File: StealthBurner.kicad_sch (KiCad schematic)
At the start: 11 parts, among them J1 PROBE, J2 E-Step, J3 HE, J4 HET, J5 FS, J6 HEF, J7 PCF, J8 LED, J9 MCU

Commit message: 修改设计规范
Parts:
- D1: footprint (none) -> Diode_THT:D_DO-34_SOD68_P2.54mm_Vertical_AnodeUp
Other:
- company: (none) -> LassiCat Organization
- title: (none) -> StealthBurner Toolhead PCB
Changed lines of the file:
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@@
 (kicad_sch (version 20211123) (generator eeschema)
   (paper "A4")
+  (title_block
+    (title "StealthBurner Toolhead PCB")
+    (date "2022-05-24")
+    (rev "Bata0")
+    (company "LassiCat Organization")
+    (comment 1 "Auther: CharlieYu")
+  )
   (wire (pts (xy 130.81 119.38) (xy 135.89 119.38))
     (stroke (width 0) (type default) (color 0 0 0 0))
@@
     (property "Reference" "D1" (id 0) (at 133.35 66.04 0))
     (property "Value" "BAT85" (id 1) (at 134.62 67.31 0))
-    (property "Footprint" "" (id 2) (at 129.54 62.23 0)
-      (effects (font (size 1.27 1.27)) hide)
-    )
+    (property "Footprint" "Diode_THT:D_DO-34_SOD68_P2.54mm_Vertical_AnodeUp" (id 2) (at 129.54 62.23 0)
+      (effects (font (size 1.27 1.27)) hide)
+    )

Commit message: 重新设计 PCB
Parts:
- D1: footprint Diode_THT:D_DO-34_SOD68_P2.54mm_Vertical_AnodeUp -> Diode_THT:D_DO-35_SOD27_P2.54mm_Vertical_AnodeUp
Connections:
- net FS: now also J9.5 (Pin_5); no longer J9.15 (Pin_15)
- net HE+: now also J9.15 (Pin_15); no longer J9.5 (Pin_5)
- net HE-: now also J9.14 (Pin_14); no longer J9.4 (Pin_4)
- net HEF: now also J9.9 (Pin_9); no longer J9.8 (Pin_8)
- net PCF: now also J9.8 (Pin_8); no longer J9.9 (Pin_9)
- net P_SIG: now also J9.4 (Pin_4); no longer J9.14 (Pin_14)
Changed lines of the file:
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@@
     (effects (font (size 1.27 1.27)) (justify left bottom))
   )
-  (label "HE+" (at 172.72 104.775 0)
+  (label "FS" (at 172.72 104.775 0)
     (effects (font (size 1.27 1.27)) (justify left bottom))
   )
@@
     (effects (font (size 1.27 1.27)) (justify left bottom))
   )
-  (label "HE-" (at 172.72 102.235 0)
+  (label "P_SIG" (at 172.72 102.235 0)
     (effects (font (size 1.27 1.27)) (justify left bottom))
   )
@@
     (effects (font (size 1.27 1.27)) (justify right bottom))
   )
-  (label "PCF" (at 172.72 114.935 0)
+  (label "HEF" (at 172.72 114.935 0)
     (effects (font (size 1.27 1.27)) (justify left bottom))
   )
@@
     (effects (font (size 1.27 1.27)) (justify left bottom))
   )
-  (label "P_SIG" (at 195.58 104.775 180)
+  (label "HE-" (at 195.58 104.775 180)
     (effects (font (size 1.27 1.27)) (justify right bottom))
   )
@@
     (effects (font (size 1.27 1.27)) (justify left bottom))
   )
-  (label "HEF" (at 172.72 112.395 0)
+  (label "PCF" (at 172.72 112.395 0)
     (effects (font (size 1.27 1.27)) (justify left bottom))
   )
@@
     (effects (font (size 1.27 1.27)) (justify left bottom))
   )
-  (label "FS" (at 195.58 107.315 180)
+  (label "HE+" (at 195.58 107.315 180)
     (effects (font (size 1.27 1.27)) (justify right bottom))
   )
@@
     (property "Reference" "D1" (id 0) (at 133.35 66.04 0))
     (property "Value" "BAT85" (id 1) (at 134.62 67.31 0))
-    (property "Footprint" "Diode_THT:D_DO-34_SOD68_P2.54mm_Vertical_AnodeUp" (id 2) (at 129.54 62.23 0)
+    (property "Footprint" "Diode_THT:D_DO-35_SOD27_P2.54mm_Vertical_AnodeUp" (id 2) (at 129.54 62.23 0)
       (effects (font (size 1.27 1.27)) hide)
     )
@@
     )
     (path "/9a063b19-e5f3-48b5-bbc2-933e767ffdb2"
-      (reference "D1") (unit 1) (value "BAT85") (footprint "Diode_THT:D_DO-34_SOD68_P2.54mm_Vertical_AnodeUp")
+      (reference "D1") (unit 1) (value "BAT85") (footprint "Diode_THT:D_DO-35_SOD27_P2.54mm_Vertical_AnodeUp")
     )
     (path "/eb9a0309-9ad7-454e-b1f6-0754790b2de6"

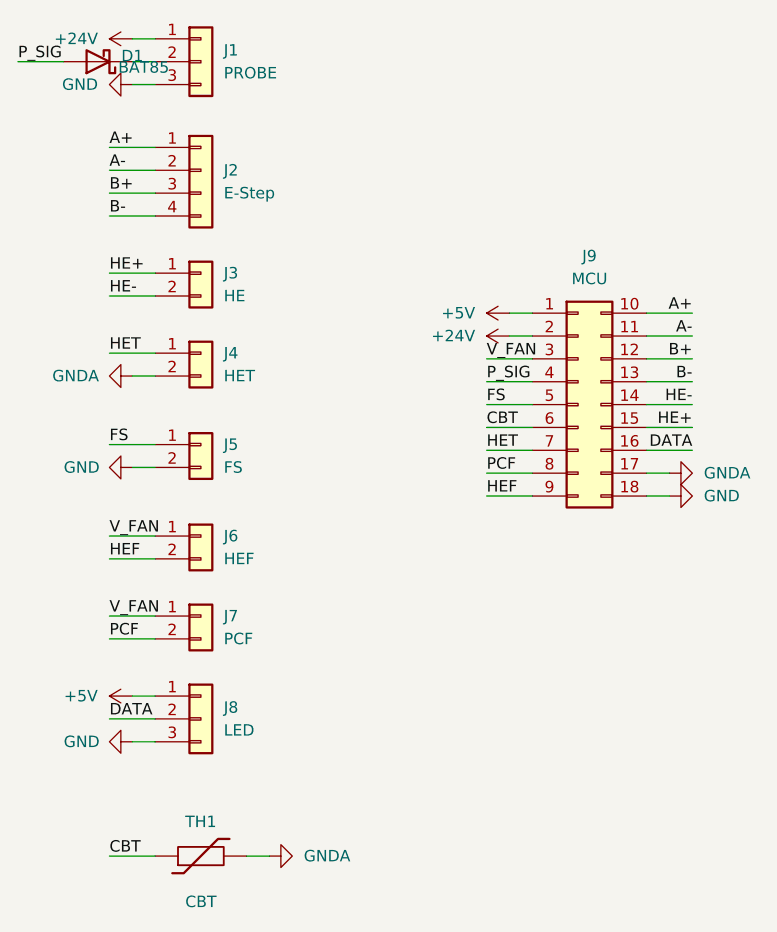
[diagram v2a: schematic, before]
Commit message: 更新到 Beta2，优化探针接口位置，优化丝印
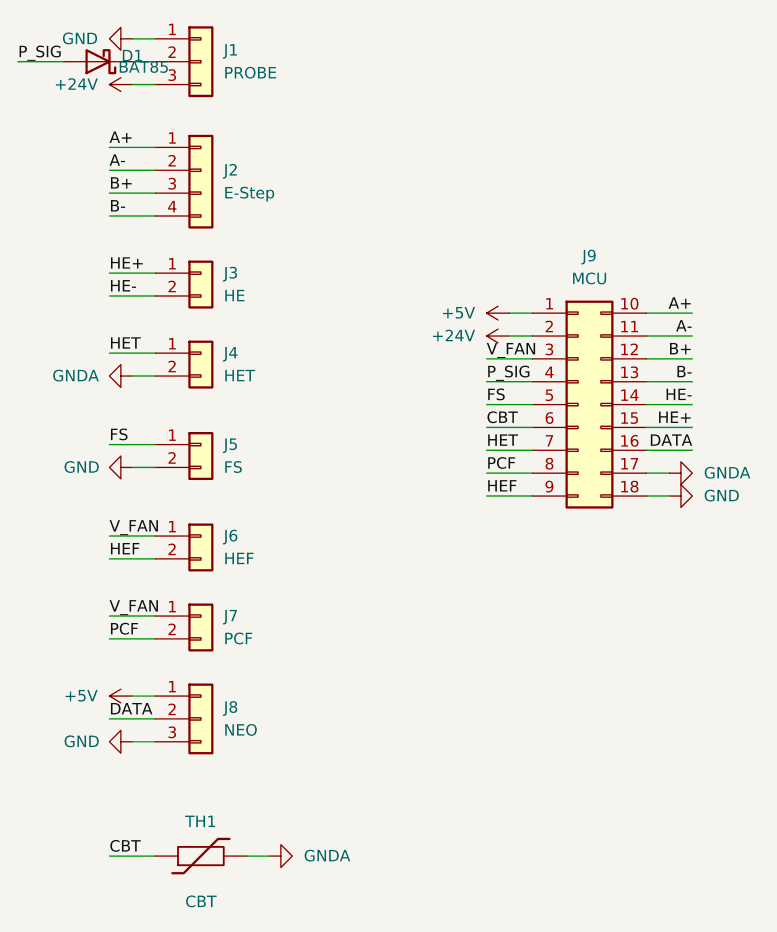
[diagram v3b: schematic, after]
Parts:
- J8: value LED -> NEO
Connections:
- net +24V: now also J1.3 (Pin_3); no longer J1.1 (Pin_1)
- net GND: now also J1.1 (Pin_1); no longer J1.3 (Pin_3)
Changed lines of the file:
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@@
   (title_block
     (title "StealthBurner Toolhead PCB")
-    (date "2022-05-24")
-    (rev "Bata0")
+    (date "2022-06-02")
+    (rev "Bata2")
     (company "LassiCat Organization")
     (comment 1 "Auther: CharlieYu")
@@
     (pin "1")
   )
-  (symbol (lib_id "power:+24V") (at 133.35 64.135 90) (unit 1)
-    (in_bom yes) (on_board yes) (fields_autoplaced)
-    (property "Reference" "#PWR01" (id 0) (at 137.16 64.135 0)
-      (effects (font (size 1.27 1.27)) hide)
-    )
-    (property "Value" "+24V" (id 1) (at 129.54 64.1349 90)
-      (effects (font (size 1.27 1.27)) (justify left))
-    )
-    (property "Footprint" "" (id 2) (at 133.35 64.135 0)
-      (effects (font (size 1.27 1.27)) hide)
-    )
-    (property "Datasheet" "" (id 3) (at 133.35 64.135 0)
+  (symbol (lib_id "power:+24V") (at 133.35 69.215 90) (unit 1)
+    (in_bom yes) (on_board yes) (fields_autoplaced)
+    (property "Reference" "#PWR01" (id 0) (at 137.16 69.215 0)
+      (effects (font (size 1.27 1.27)) hide)
+    )
+    (property "Value" "+24V" (id 1) (at 129.54 69.2149 90)
+      (effects (font (size 1.27 1.27)) (justify left))
+    )
+    (property "Footprint" "" (id 2) (at 133.35 69.215 0)
+      (effects (font (size 1.27 1.27)) hide)
+    )
+    (property "Datasheet" "" (id 3) (at 133.35 69.215 0)
       (effects (font (size 1.27 1.27)) hide)
     )
@@
     (pin "1")
   )
-  (symbol (lib_id "power:GND") (at 133.35 69.215 270) (unit 1)
-    (in_bom yes) (on_board yes) (fields_autoplaced)
-    (property "Reference" "#PWR02" (id 0) (at 127 69.215 0)
-      (effects (font (size 1.27 1.27)) hide)
-    )
-    (property "Value" "GND" (id 1) (at 129.54 69.2149 90)
+  (symbol (lib_id "power:GND") (at 133.35 64.135 270) (unit 1)
+    (in_bom yes) (on_board yes) (fields_autoplaced)
+    (property "Reference" "#PWR02" (id 0) (at 127 64.135 0)
+      (effects (font (size 1.27 1.27)) hide)
+    )
+    (property "Value" "GND" (id 1) (at 129.54 64.1349 90)
       (effects (font (size 1.27 1.27)) (justify right))
     )
-    (property "Footprint" "" (id 2) (at 133.35 69.215 0)
-      (effects (font (size 1.27 1.27)) hide)
-    )
-    (property "Datasheet" "" (id 3) (at 133.35 69.215 0)
+    (property "Footprint" "" (id 2) (at 133.35 64.135 0)
+      (effects (font (size 1.27 1.27)) hide)
+    )
+    (property "Datasheet" "" (id 3) (at 133.35 64.135 0)
       (effects (font (size 1.27 1.27)) hide)
     )
@@
       (effects (font (size 1.27 1.27)) (justify left))
     )
-    (property "Value" "LED" (id 1) (at 143.51 140.9699 0)
+    (property "Value" "NEO" (id 1) (at 143.51 140.9699 0)
       (effects (font (size 1.27 1.27)) (justify left))
     )
@@
     )
     (path "/ef798567-f028-441c-9db5-6e1810d5a9a5"
-      (reference "J8") (unit 1) (value "LED") (footprint "Connector_JST:JST_PH_B3B-PH-K_1x03_P2.00mm_Vertical")
+      (reference "J8") (unit 1) (value "NEO") (footprint "Connector_JST:JST_PH_B3B-PH-K_1x03_P2.00mm_Vertical")
     )
     (path "/7c97d781-16eb-458a-91a2-bfecfd5fd580"

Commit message: 更改线路名称
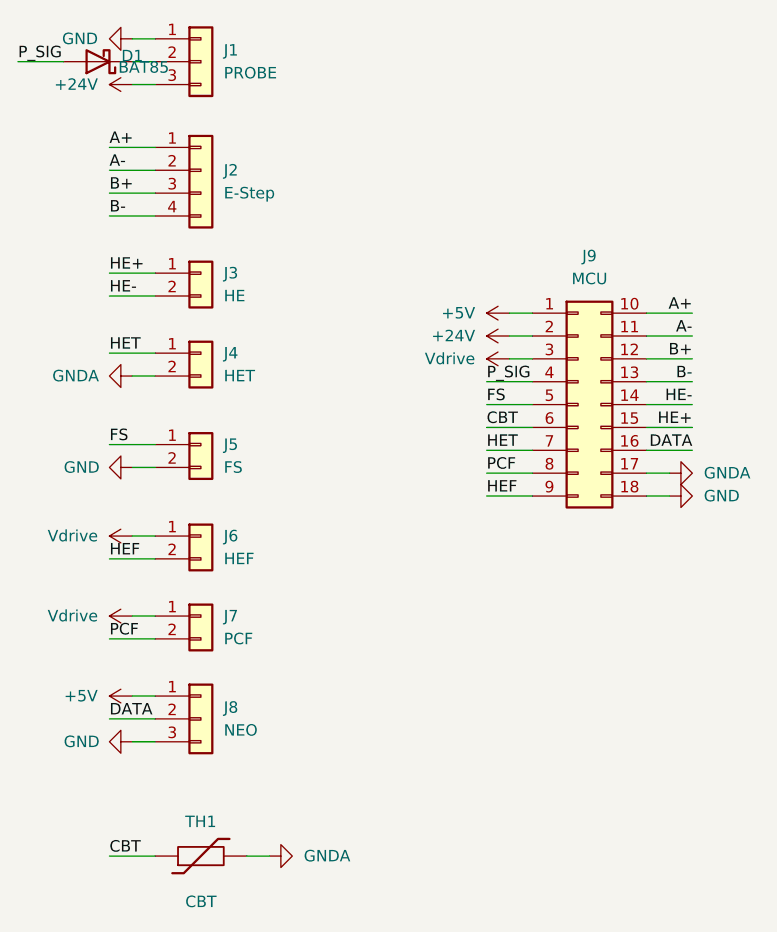
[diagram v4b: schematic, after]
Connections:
- net V_FAN renamed Vdrive
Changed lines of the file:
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@@
     (comment 1 "Auther: CharlieYu")
   )
-  (wire (pts (xy 130.81 119.38) (xy 135.89 119.38))
+  (wire (pts (xy 133.35 119.38) (xy 135.89 119.38))
     (stroke (width 0) (type default) (color 0 0 0 0))
   )
@@
     (stroke (width 0) (type default) (color 0 0 0 0))
   )
-  (wire (pts (xy 172.72 99.695) (xy 177.8 99.695))
+  (wire (pts (xy 175.26 99.695) (xy 177.8 99.695))
     (stroke (width 0) (type default) (color 0 0 0 0))
   )
@@
     (stroke (width 0) (type default) (color 0 0 0 0))
   )
-  (wire (pts (xy 130.81 128.27) (xy 135.89 128.27))
+  (wire (pts (xy 133.35 128.27) (xy 135.89 128.27))
     (stroke (width 0) (type default) (color 0 0 0 0))
   )
@@
     (effects (font (size 1.27 1.27)) (justify right bottom))
   )
-  (label "V_FAN" (at 130.81 119.38 0)
-    (effects (font (size 1.27 1.27)) (justify left bottom))
-  )
   (label "HET" (at 130.81 99.06 0)
     (effects (font (size 1.27 1.27)) (justify left bottom))
@@
   )
   (label "PCF" (at 130.81 130.81 0)
-    (effects (font (size 1.27 1.27)) (justify left bottom))
-  )
-  (label "V_FAN" (at 172.72 99.695 0)
-    (effects (font (size 1.27 1.27)) (justify left bottom))
-  )
-  (label "V_FAN" (at 130.81 128.27 0)
     (effects (font (size 1.27 1.27)) (justify left bottom))
   )
@@
     (pin "4")
   )
+  (symbol (lib_id "power:Vdrive") (at 133.35 128.27 90) (unit 1)
+    (in_bom yes) (on_board yes) (fields_autoplaced)
+    (property "Reference" "#PWR0102" (id 0) (at 137.16 133.35 0)
+      (effects (font (size 1.27 1.27)) hide)
+    )
+    (property "Value" "Vdrive" (id 1) (at 129.54 128.2699 90)
+      (effects (font (size 1.27 1.27)) (justify left))
+    )
+    (property "Footprint" "" (id 2) (at 133.35 128.27 0)
+      (effects (font (size 1.27 1.27)) hide)
+    )
+    (property "Datasheet" "" (id 3) (at 133.35 128.27 0)
+      (effects (font (size 1.27 1.27)) hide)
+    )
+    (pin "1")
+  )
   (symbol (lib_id "power:+24V") (at 175.26 97.155 90) (unit 1)
     (in_bom yes) (on_board yes) (fields_autoplaced)
@@
     (pin "2")
   )
+  (symbol (lib_id "power:Vdrive") (at 175.26 99.695 90) (unit 1)
+    (in_bom yes) (on_board yes) (fields_autoplaced)
+    (property "Reference" "#PWR0101" (id 0) (at 179.07 104.775 0)
+      (effects (font (size 1.27 1.27)) hide)
+    )
+    (property "Value" "Vdrive" (id 1) (at 171.45 99.6949 90)
+      (effects (font (size 1.27 1.27)) (justify left))
+    )
+    (property "Footprint" "" (id 2) (at 175.26 99.695 0)
+      (effects (font (size 1.27 1.27)) hide)
+    )
+    (property "Datasheet" "" (id 3) (at 175.26 99.695 0)
+      (effects (font (size 1.27 1.27)) hide)
+    )
+    (pin "1")
+  )
   (symbol (lib_id "Connector_Generic:Conn_01x02") (at 140.97 90.17 0) (unit 1)
     (in_bom yes) (on_board yes) (fields_autoplaced)
@@
     (pin "1")
   )
+  (symbol (lib_id "power:Vdrive") (at 133.35 119.38 90) (unit 1)
+    (in_bom yes) (on_board yes) (fields_autoplaced)
+    (property "Reference" "#PWR0103" (id 0) (at 137.16 124.46 0)
+      (effects (font (size 1.27 1.27)) hide)
+    )
+    (property "Value" "Vdrive" (id 1) (at 129.54 119.3799 90)
+      (effects (font (size 1.27 1.27)) (justify left))
+    )
+    (property "Footprint" "" (id 2) (at 133.35 119.38 0)
+      (effects (font (size 1.27 1.27)) hide)
+    )
+    (property "Datasheet" "" (id 3) (at 133.35 119.38 0)
+      (effects (font (size 1.27 1.27)) hide)
+    )
+    (pin "1")
+  )
   (symbol (lib_id "power:+5V") (at 175.26 94.615 90) (unit 1)
     (in_bom yes) (on_board yes) (fields_autoplaced)
@@
       (reference "#PWR011") (unit 1) (value "GND") (footprint "")
     )
+    (path "/afdcc35f-02b6-45a8-9e12-2a571569a5f2"
+      (reference "#PWR0101") (unit 1) (value "Vdrive") (footprint "")
+    )
+    (path "/92e63f46-a4ca-450c-a272-84e899c867fd"
+      (reference "#PWR0102") (unit 1) (value "Vdrive") (footprint "")
+    )
+    (path "/d890e9b8-5d51-4f74-b671-7a86eaa60577"
+      (reference "#PWR0103") (unit 1) (value "Vdrive") (footprint "")
+    )
     (path "/9a063b19-e5f3-48b5-bbc2-933e767ffdb2"
